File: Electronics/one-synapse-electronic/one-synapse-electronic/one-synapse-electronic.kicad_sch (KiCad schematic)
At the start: 40 parts, among them J1 synapses, J2 Conn_01x08_Socket, J3 Conn_01x08_Socket, J4 Conn_01x07_Socket, J5 Conn_01x07_Pin, J6 Conn_01x02_Pin, Q1 BS170F, Q10 BS170F, Q11 BS170F, Q12 BS170F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

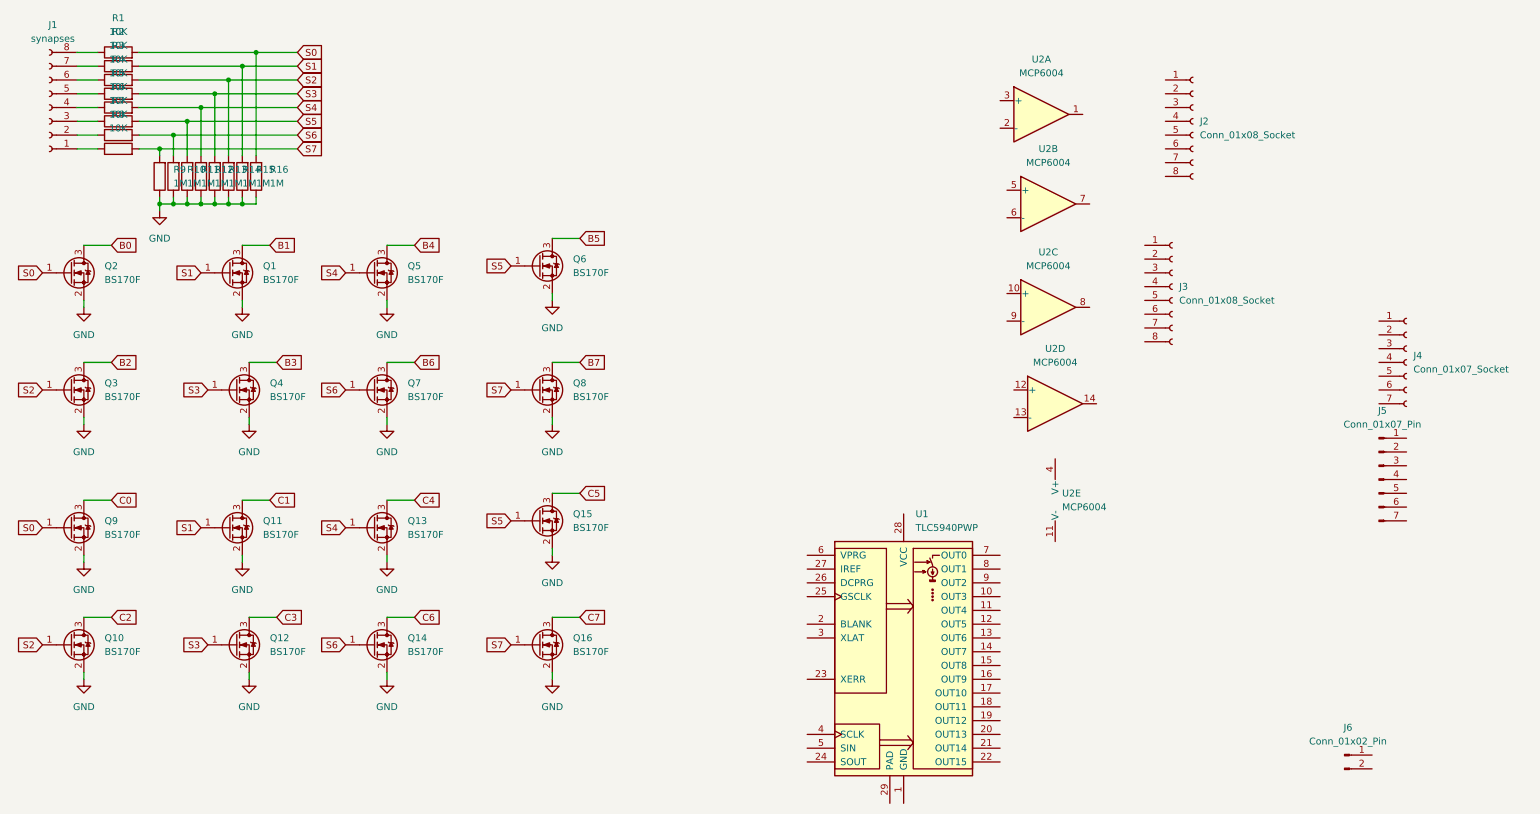
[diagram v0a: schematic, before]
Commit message: Initial design for analogue electronic synapse
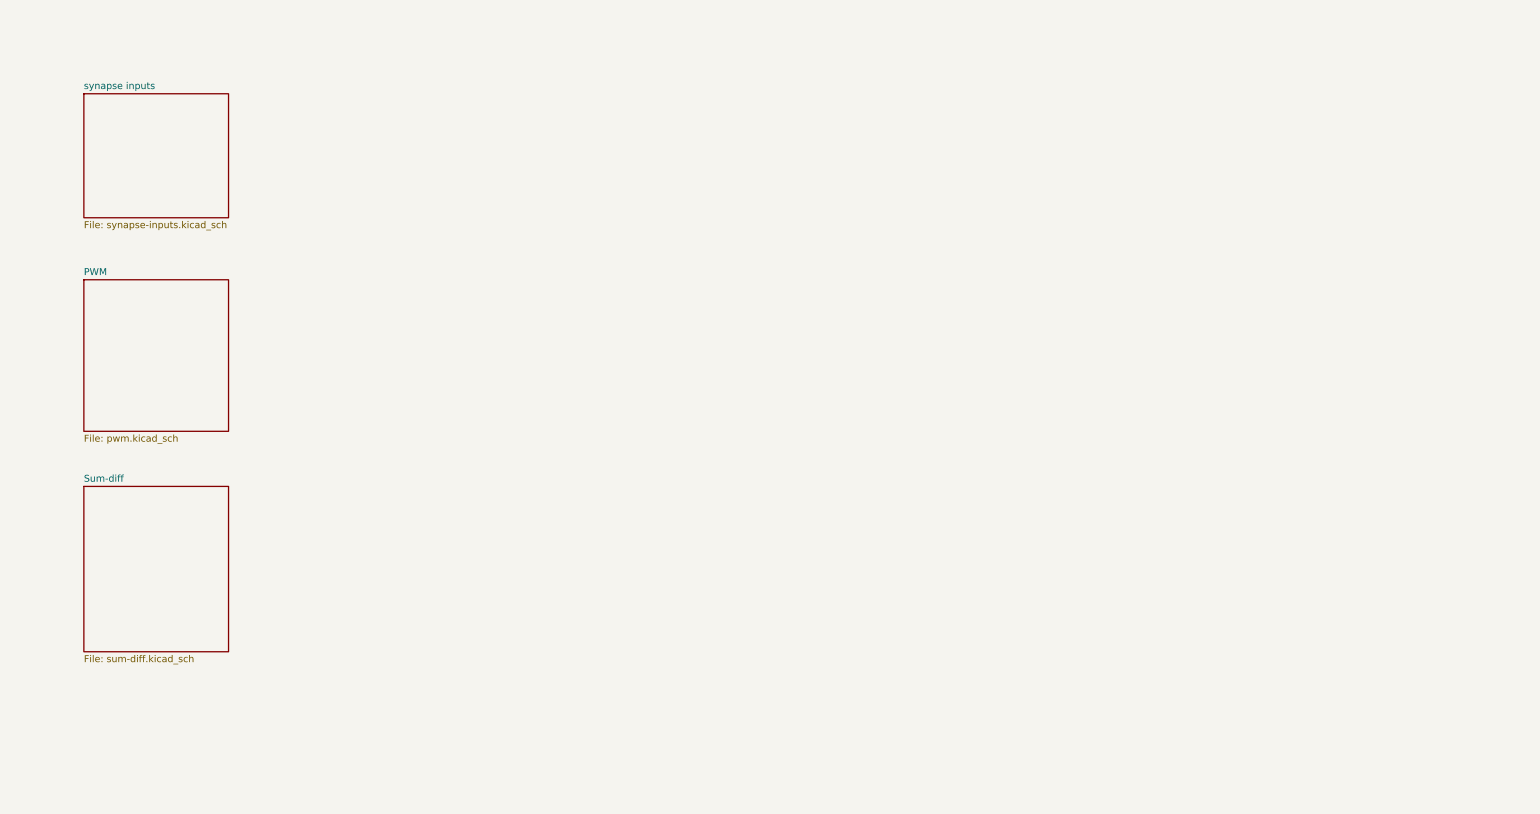
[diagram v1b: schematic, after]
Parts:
- removed J1: synapses, Connector_PinHeader_2.54mm:PinHeader_1x08_P2.54mm_Vertical, symbol Connector:Conn_01x08_Socket
- removed J2, J3: Conn_01x08_Socket, symbol Connector:Conn_01x08_Socket
- removed J4: Conn_01x07_Socket, symbol Connector:Conn_01x07_Socket
- removed J5: Conn_01x07_Pin, symbol Connector:Conn_01x07_Pin
- removed J6: Conn_01x02_Pin, symbol Connector:Conn_01x02_Pin
- removed Q1, Q10, Q11, Q12, Q13, Q14, Q15, Q16, Q2, Q3, Q4, Q5, Q6, Q7, Q8, Q9: BS170F, Package_TO_SOT_SMD:SOT-23, symbol Transistor_FET:BS170F
- removed R1, R2, R3, R4, R5, R6, R7, R8: 10K, Resistor_SMD:R_0805_2012Metric, symbol Device:R
- removed R10, R11, R12, R13, R14, R15, R16, R9: 1M, Resistor_SMD:R_0805_2012Metric, symbol Device:R
- removed U1: TLC5940PWP, Package_SO:HTSSOP-28-1EP_4.4x9.7mm_P0.65mm_EP3.4x9.5mm_Mask2.4x6.17mm_ThermalVias, symbol Driver_LED:TLC5940PWP
- removed U2: MCP6004, symbol Amplifier_Operational:MCP6004
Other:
- added sheet PWM (pwm.kicad_sch)
- added sheet Sum-diff (sum-diff.kicad_sch)
- added sheet synapse inputs (synapse-inputs.kicad_sch)

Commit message: WIP
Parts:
- added H1, H2, H3, H4: MountingHole, MountingHole:MountingHole_2.5mm, symbol Mechanical:MountingHole
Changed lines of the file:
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@@
 (kicad_sch (version 20230121) (generator eeschema)
   (paper "A4")
+  (symbol (lib_id "Mechanical:MountingHole") (at 69.85 44.45 0) (unit 1)
+    (in_bom yes) (on_board yes) (dnp no) (fields_autoplaced)
+    (property "Reference" "H1" (at 72.39 43.18 0)
+      (effects (font (size 1.27 1.27)) (justify left))
+    )
+    (property "Value" "MountingHole" (at 72.39 45.72 0)
+      (effects (font (size 1.27 1.27)) (justify left))
+    )
+    (property "Footprint" "MountingHole:MountingHole_2.5mm" (at 69.85 44.45 0)
+      (effects (font (size 1.27 1.27)) hide)
+    )
+    (property "Datasheet" "~" (at 69.85 44.45 0)
+      (effects (font (size 1.27 1.27)) hide)
+    )
+    (instances
+      (project "one-synapse-electronic"
+        (path "/133ffd0f-a451-425f-8ce0-4540f5afe04a"
+          (reference "H1") (unit 1)
+        )
+      )
+    )
+  )
+  (symbol (lib_id "Mechanical:MountingHole") (at 69.85 69.85 0) (unit 1)
+    (in_bom yes) (on_board yes) (dnp no) (fields_autoplaced)
+    (property "Reference" "H4" (at 72.39 68.58 0)
+      (effects (font (size 1.27 1.27)) (justify left))
+    )
+    (property "Value" "MountingHole" (at 72.39 71.12 0)
+      (effects (font (size 1.27 1.27)) (justify left))
+    )
+    (property "Footprint" "MountingHole:MountingHole_2.5mm" (at 69.85 69.85 0)
+      (effects (font (size 1.27 1.27)) hide)
+    )
+    (property "Datasheet" "~" (at 69.85 69.85 0)
+      (effects (font (size 1.27 1.27)) hide)
+    )
+    (instances
+      (project "one-synapse-electronic"
+        (path "/133ffd0f-a451-425f-8ce0-4540f5afe04a"
+          (reference "H4") (unit 1)
+        )
+      )
+    )
+  )
+  (symbol (lib_id "Mechanical:MountingHole") (at 69.85 60.96 0) (unit 1)
+    (in_bom yes) (on_board yes) (dnp no) (fields_autoplaced)
+    (property "Reference" "H3" (at 72.39 59.69 0)
+      (effects (font (size 1.27 1.27)) (justify left))
+    )
+    (property "Value" "MountingHole" (at 72.39 62.23 0)
+      (effects (font (size 1.27 1.27)) (justify left))
+    )
+    (property "Footprint" "MountingHole:MountingHole_2.5mm" (at 69.85 60.96 0)
+      (effects (font (size 1.27 1.27)) hide)
+    )
+    (property "Datasheet" "~" (at 69.85 60.96 0)
+      (effects (font (size 1.27 1.27)) hide)
+    )
+    (instances
+      (project "one-synapse-electronic"
+        (path "/133ffd0f-a451-425f-8ce0-4540f5afe04a"
+          (reference "H3") (unit 1)
+        )
+      )
+    )
+  )
+  (symbol (lib_id "Mechanical:MountingHole") (at 69.85 53.34 0) (unit 1)
+    (in_bom yes) (on_board yes) (dnp no) (fields_autoplaced)
+    (property "Reference" "H2" (at 72.39 52.07 0)
+      (effects (font (size 1.27 1.27)) (justify left))
+    )
+    (property "Value" "MountingHole" (at 72.39 54.61 0)
+      (effects (font (size 1.27 1.27)) (justify left))
+    )
+    (property "Footprint" "MountingHole:MountingHole_2.5mm" (at 69.85 53.34 0)
+      (effects (font (size 1.27 1.27)) hide)
+    )
+    (property "Datasheet" "~" (at 69.85 53.34 0)
+      (effects (font (size 1.27 1.27)) hide)
+    )
+    (instances
+      (project "one-synapse-electronic"
+        (path "/133ffd0f-a451-425f-8ce0-4540f5afe04a"
+          (reference "H2") (unit 1)
+        )
+      )
+    )
+  )
   (sheet (at 30.48 30.48) (size 26.67 22.86) (fields_autoplaced)
     (stroke (width 0.1524) (type solid))
